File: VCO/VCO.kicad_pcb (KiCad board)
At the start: 2 copper layers, 162.2 x 104.5 mm, 154 parts, among them J101 Conn_02x05_Odd_Even, J201 AudioJack2_SwitchT, J202 AudioJack2_SwitchT, J203 AudioJack2_SwitchT, J204 AudioJack2_SwitchT, J301 AudioJack2_SwitchT, J401 AudioJack2_SwitchT, J402 AudioJack2_SwitchT, J501 AudioJack2_SwitchT, J502 AudioJack2_SwitchT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

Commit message: Fix VCO design rule errors
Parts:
- RV205, RV206, RV301, RV302, RV403, RV501, RV502, RV601: footprint Potentiometer_THT:Potentiometer_Runtron_RM-065_Vertical -> Custom:Potentiometer_Runtron_RM-065_Vertical_Improved
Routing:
- net Net-(R406-Pad2): track 27.6 -> 27.1 mm

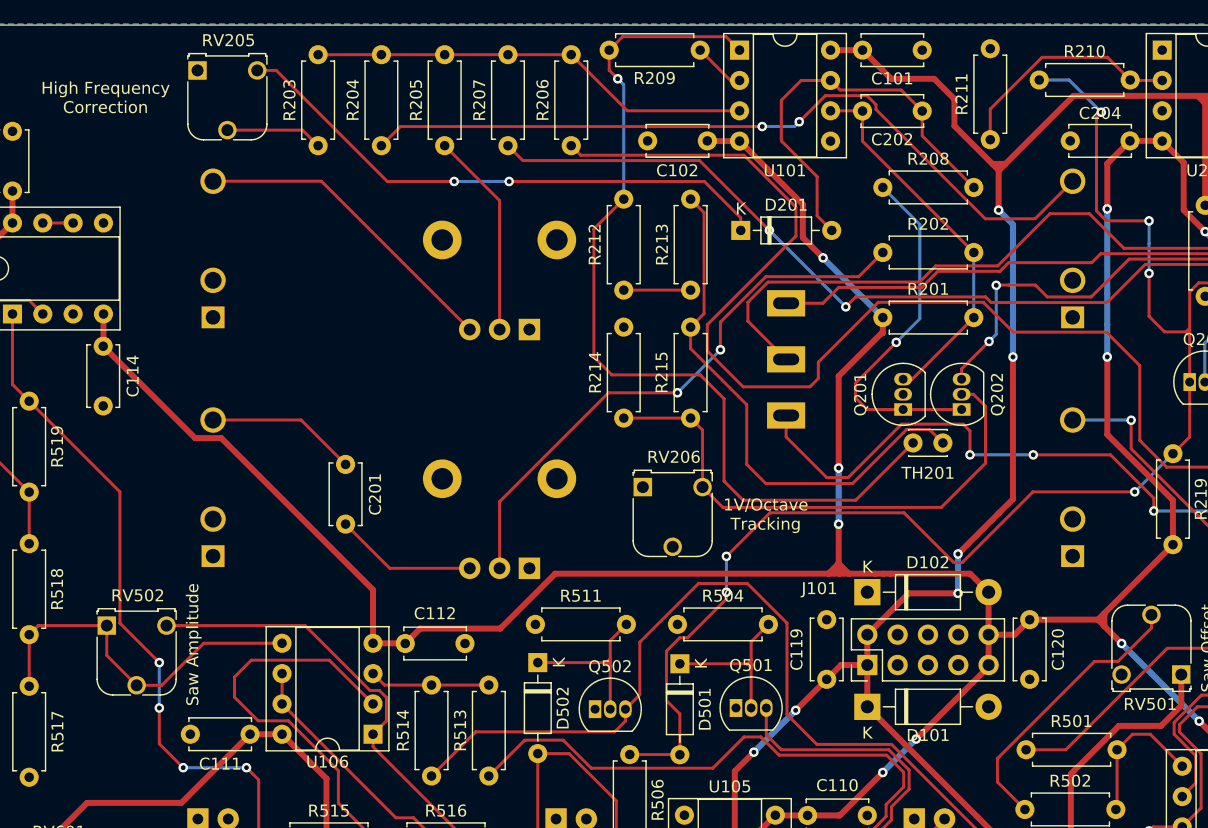
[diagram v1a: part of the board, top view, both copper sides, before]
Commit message: Apply VCO changes to PCB layout
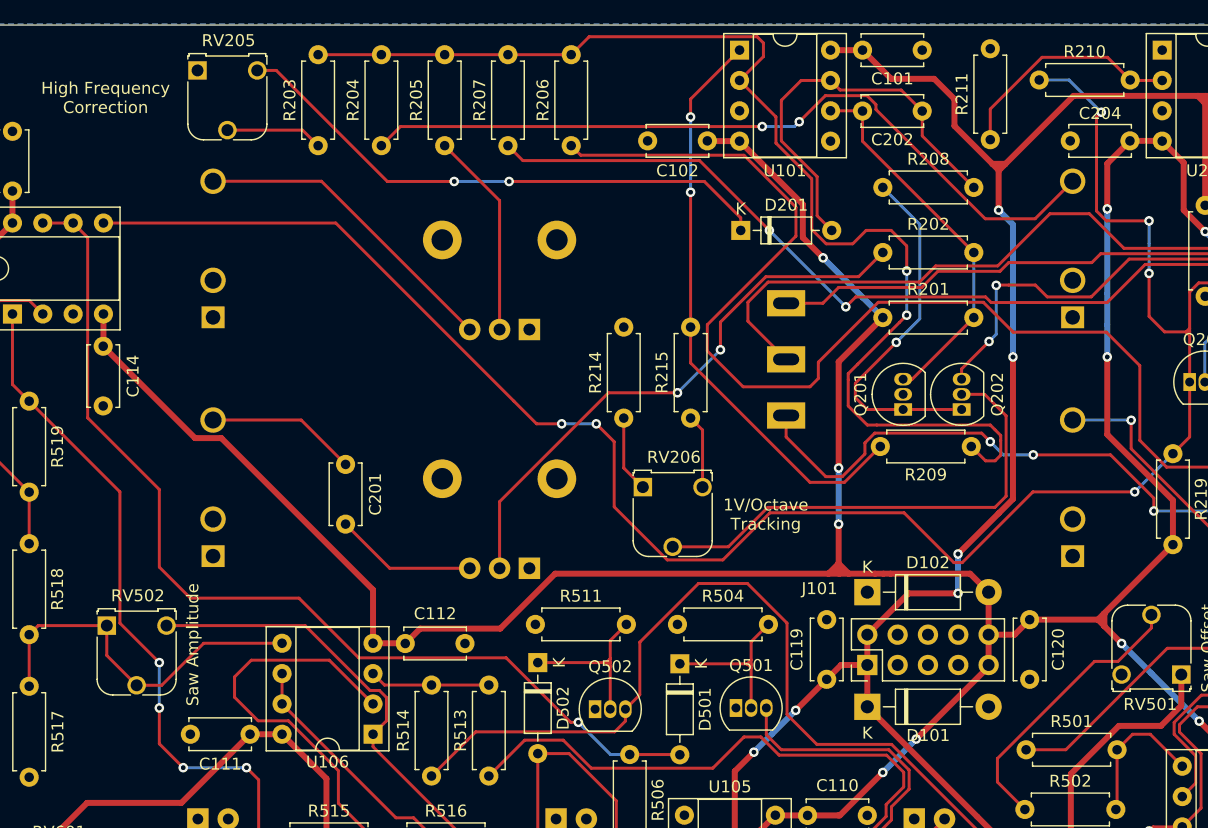
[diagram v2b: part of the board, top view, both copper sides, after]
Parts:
- removed R212: 10k, Resistor_THT:R_Axial_DIN0207_L6.3mm_D2.5mm_P7.62mm_Horizontal
- removed R213: 1k, Resistor_THT:R_Axial_DIN0207_L6.3mm_D2.5mm_P7.62mm_Horizontal
- removed TH201: 10k, Thermistor:THERM_MF52-103
- R202: value 1M -> 8.2k
- R203: value 2M -> 330k
- R209: value 22k -> 2k
- R214: value 4.7k -> 820
- R215: value 22k -> 47
- R613, R614, R615, R616: value 150k -> 75k
- RV206: value 10k -> 100
- moved R209 40.2 mm to (169.2, 70.7)
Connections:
- D501 pad 2: /Base/Square -> Net-(D501-Pad2)
- J201 pad TN: Net-(J201-PadTN) -> unconnected-(J201-PadTN)
- J202 pad TN: Net-(J202-PadTN) -> unconnected-(J202-PadTN)
- J203 pad TN: Net-(J203-PadTN) -> unconnected-(J203-PadTN)
- J204 pad TN: Net-(J204-PadTN) -> unconnected-(J204-PadTN)
- J301 pad TN: Net-(J301-PadTN) -> unconnected-(J301-PadTN)
- J401 pad TN: Net-(J401-PadTN) -> unconnected-(J401-PadTN)
- J402 pad TN: Net-(J402-PadTN) -> unconnected-(J402-PadTN)
- J501 pad TN: Net-(J501-PadTN) -> unconnected-(J501-PadTN)
- J502 pad TN: Net-(J502-PadTN) -> unconnected-(J502-PadTN)
- R209 pad 1: Net-(R209-Pad1) -> Net-(R203-Pad2)
- R214 pad 1: Net-(Q202-Pad2) -> Net-(R214-Pad1)
- R215 pad 1: Net-(R213-Pad2) -> Net-(R209-Pad2)
- R215 pad 2: Net-(Q202-Pad2) -> Net-(R215-Pad2)
- R506 pad 1: /Base/Square -> Net-(D501-Pad2)
- RV206 pad 1: GND -> Net-(R214-Pad1)
- RV206 pad 2: GND -> Net-(Q202-Pad2)
- RV206 pad 3: Net-(Q202-Pad2) -> Net-(R215-Pad2)
- U101 pad 2: Net-(R209-Pad1) -> Net-(R203-Pad2)
- U101 pad 3: Net-(R203-Pad2) -> GND
- U107 pad 5: GND -> /Base/Square
- U107 pad 6: Net-(U107-Pad6) -> Net-(D501-Pad2)
- U107 pad 7: Net-(U107-Pad6) -> Net-(D501-Pad2)
- U201 pad 1: Net-(U201-Pad1) -> unconnected-(U201-Pad1)
- U201 pad 8: Net-(U201-Pad8) -> unconnected-(U201-Pad8)
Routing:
- net Net-(D501-Pad2): track 0.00 -> 84.5 mm, vias 0 -> 1
- net Net-(R203-Pad2): track 37.2 -> 100.6 mm, vias 0 -> 2
- net Net-(R213-Pad2): track 44.5 -> 0.00 mm
- net /Base/Square: track 142.4 -> 185.9 mm
- net Net-(R209-Pad2): track 76.8 -> 49.2 mm, vias 1 -> 2
- net Net-(R214-Pad1): track 0.00 -> 6.44 mm
- net Net-(R215-Pad2): track 0.00 -> 6.19 mm
- net Net-(R212-Pad2): track 5.60 -> 0.00 mm
- net Net-(R209-Pad1): track 4.35 -> 0.00 mm
- net Net-(Q202-Pad2): track 44.9 -> 40.9 mm
- net Net-(U107-Pad6): track 2.54 -> 0.00 mm
- net Net-(C205-Pad1): track 99.3 -> 98.0 mm

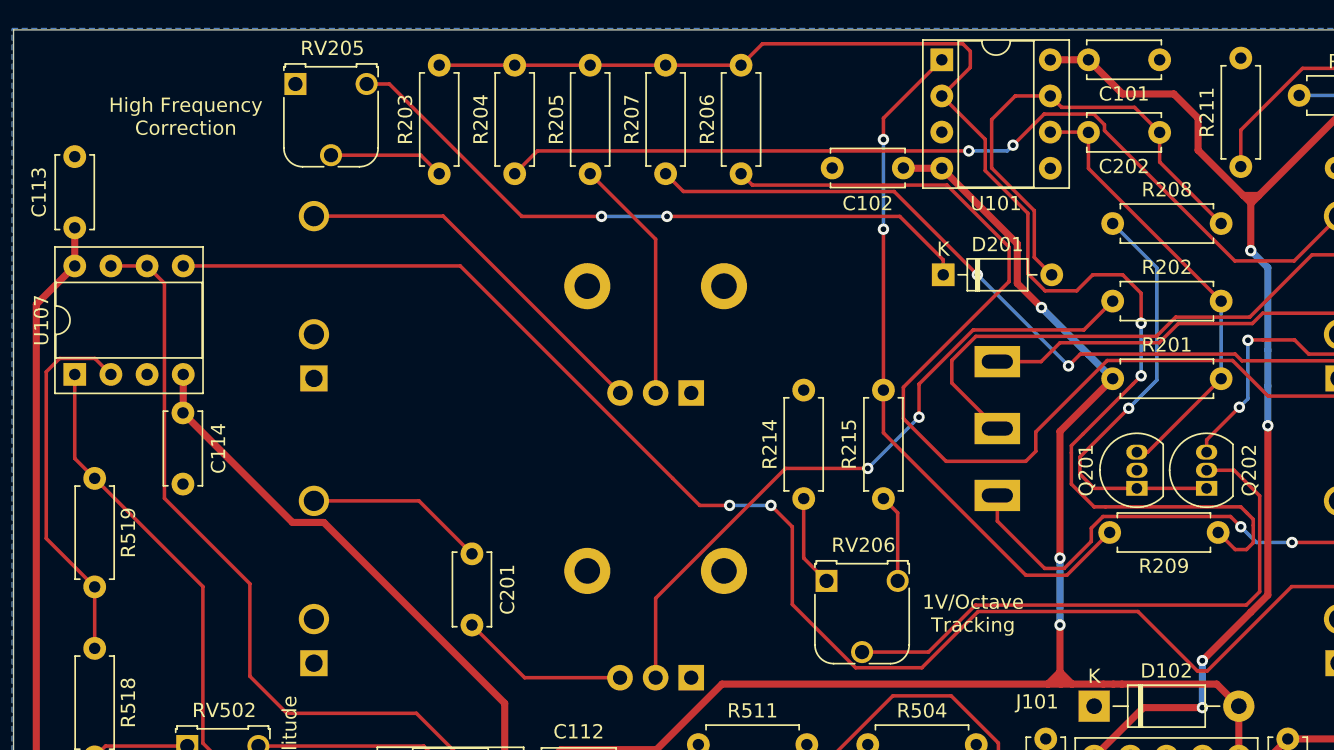
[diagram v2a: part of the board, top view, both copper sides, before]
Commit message: Change some VCO trim pot footprints
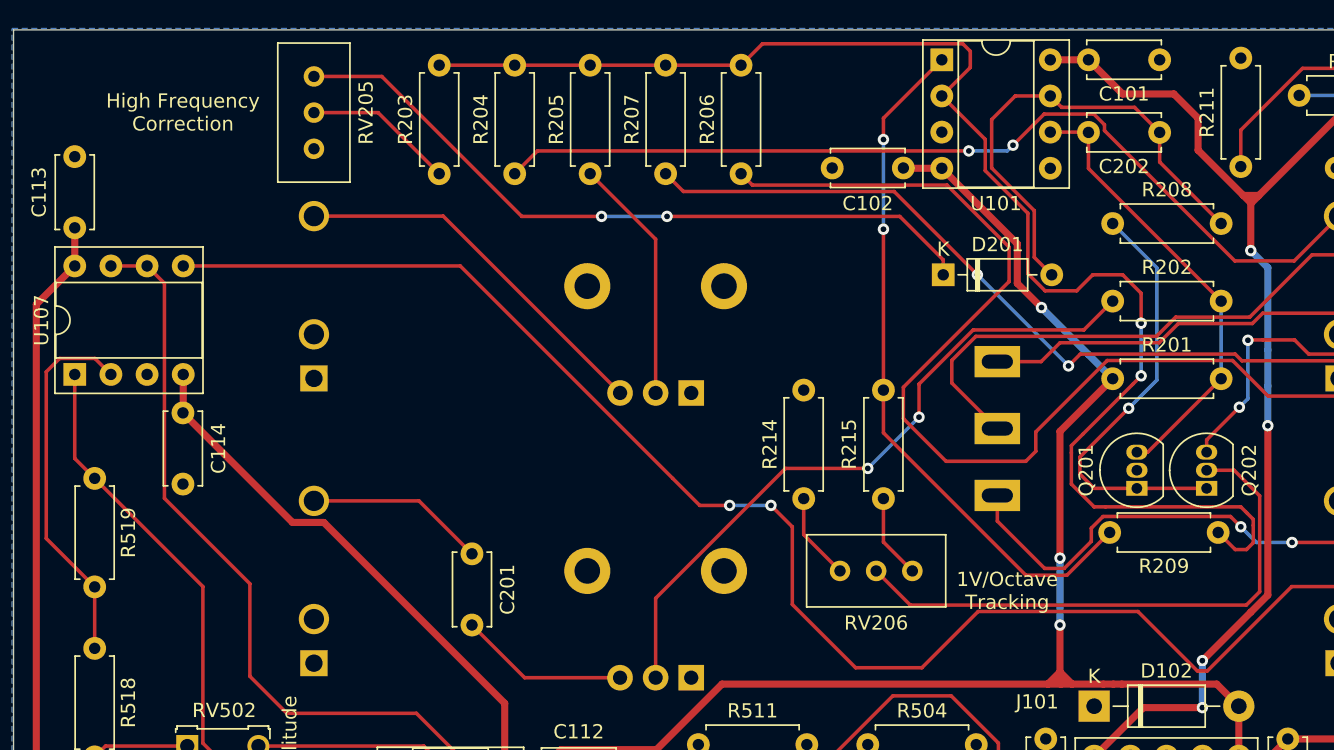
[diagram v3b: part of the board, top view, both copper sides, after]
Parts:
- R203: value 330k -> 2.2M
- RV205: value 10k -> 100k; footprint Custom:Potentiometer_Runtron_RM-065_Vertical_Improved -> Potentiometer_THT:Potentiometer_Bourns_3296W_Vertical
- RV206: footprint Custom:Potentiometer_Runtron_RM-065_Vertical_Improved -> Potentiometer_THT:Potentiometer_Bourns_3296W_Vertical
- moved RV205 4.73 mm to (105.7, 43.8), turned to -90 degrees
- moved RV206 1.18 mm to (142.7, 73.4), turned to 180 degrees
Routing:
- net Net-(D201-Pad1): track 46.7 -> 50.6 mm
- net Net-(R203-Pad1): track 8.14 -> 10.6 mm
- net Net-(Q202-Pad2): track 40.9 -> 39.5 mm

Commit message: Finish delay PCB
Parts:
- moved C207 21.3 mm to (179.7, 73.9)
- moved R221 21.3 mm to (191.2, 77.2)
- moved R403 21.3 mm to (223.9, 124.0)
- moved R501 21.3 mm to (154.2, 104.5)
- moved R509 21.3 mm to (139.9, 122.2)
- moved RV501 21.3 mm to (167.2, 98.2)
- moved R201 21.3 mm to (142.2, 68.3)
- moved R202 21.3 mm to (142.2, 62.9)
- moved R208 21.3 mm to (142.2, 57.4)
- moved R211 21.3 mm to (151.2, 53.4)
- moved R218 21.3 mm to (169.2, 58.9)
- moved U101 21.3 mm to (130.2, 45.9)
- moved Q302 21.3 mm to (222.7, 78.3)
- moved R610 21.3 mm to (160.2, 123.8)
- moved U105 21.3 mm to (133.2, 117.6)
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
